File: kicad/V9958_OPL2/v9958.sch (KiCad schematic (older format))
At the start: 21 parts, among them U1 74LS139, U2 V9958, U3 DRAM_64KX4, U4 DRAM_64KX4, U5 DRAM_64KX4, U6 DRAM_64KX4, U7 DRAM_64KX4, U8 YM3812, U9 DRAM_64KX4, Y1 21,443Mhz

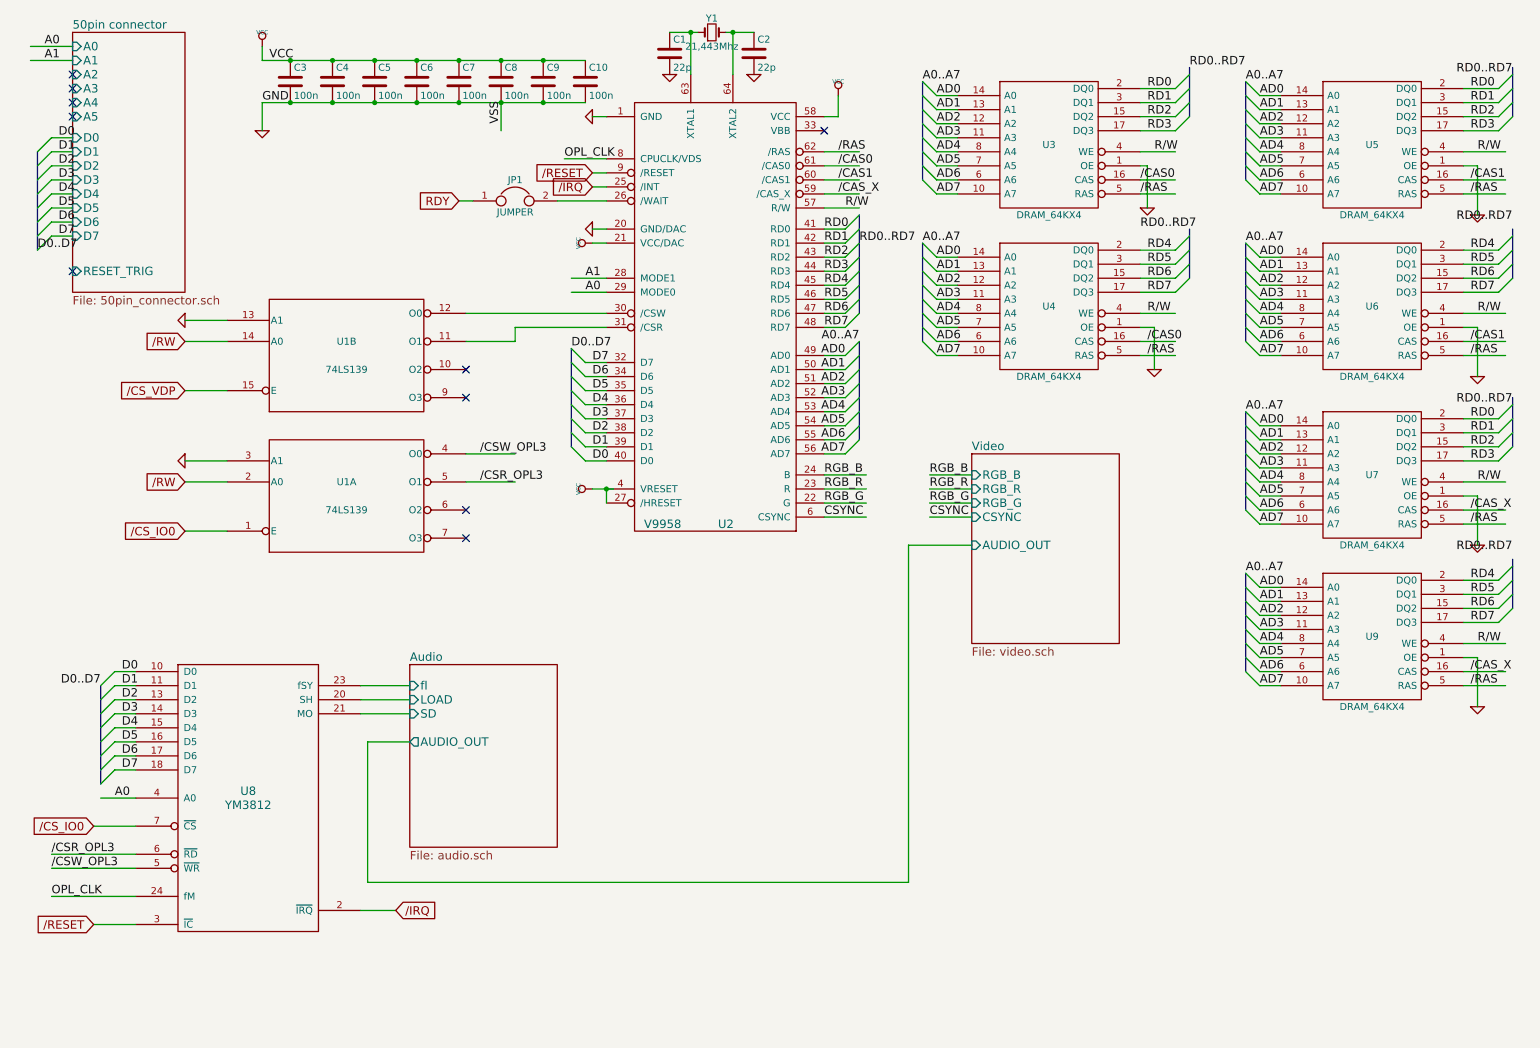
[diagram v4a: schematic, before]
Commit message: DRC fixes, filled areas
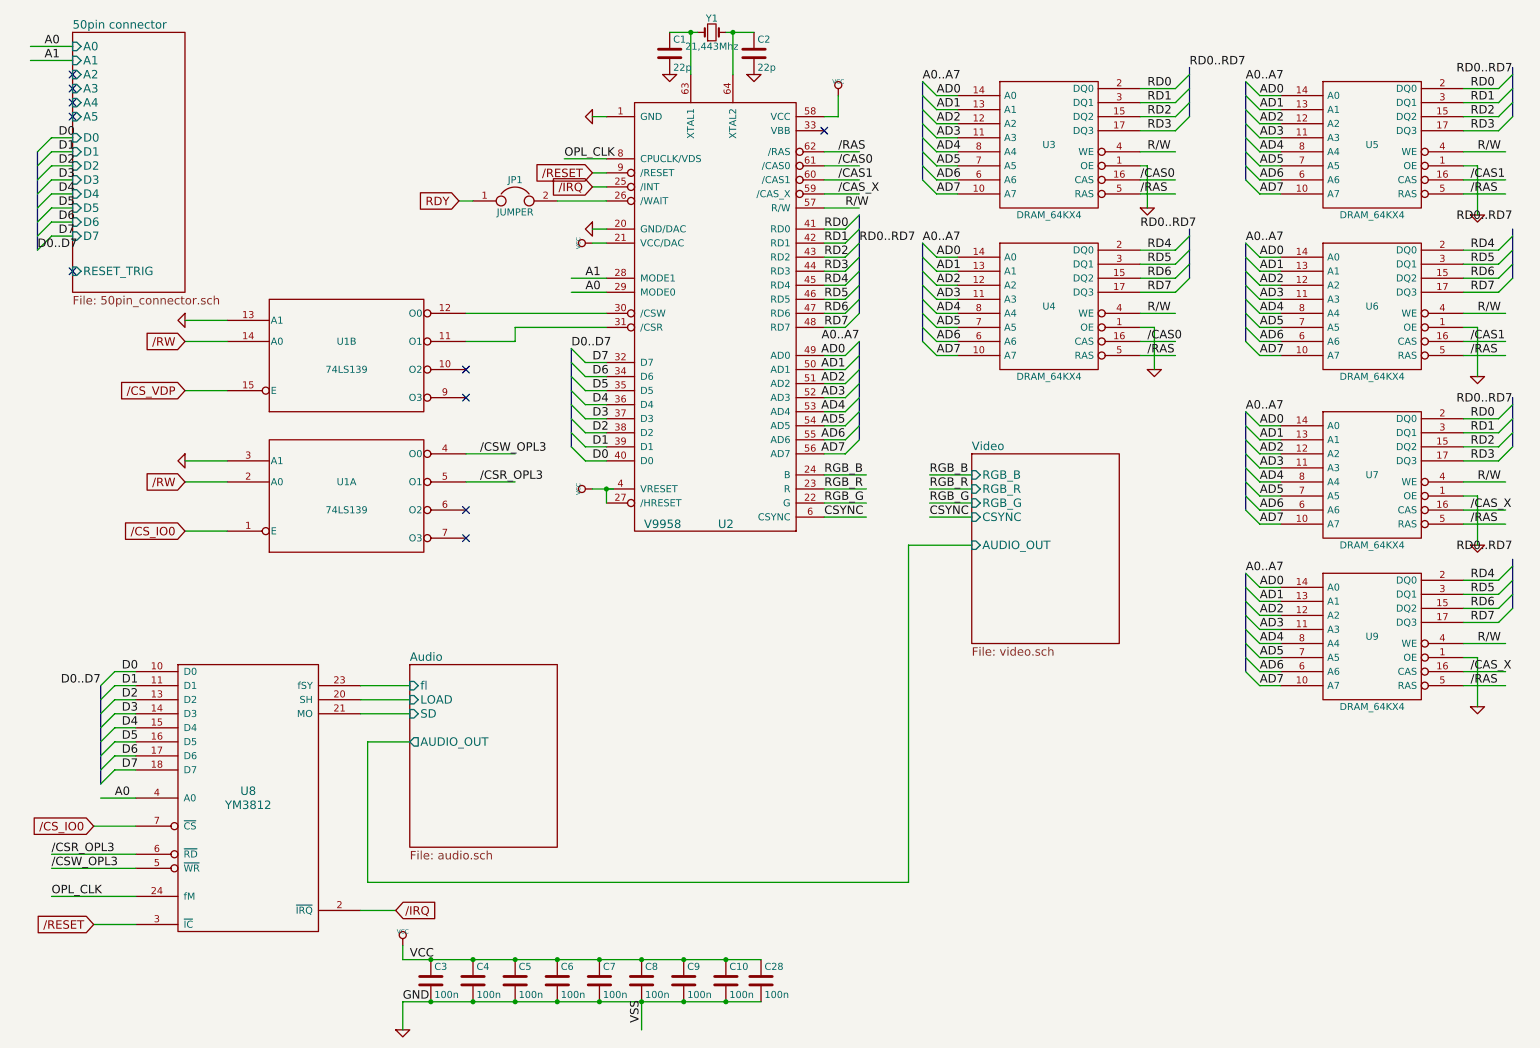
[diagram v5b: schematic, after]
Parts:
- added C28: 100n, Capacitors_ThroughHole:C_Disc_D3.0mm_W1.6mm_P2.50mm, symbol C
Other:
- moved on the sheet: C10, C3, C4, C5, C6, C7, C8, C9
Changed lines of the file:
@@
 Text Label 6350 1850 0    60   ~ 0
-R/W
-Text Label 8550 1450 0    60   ~ 0
-R/W
-Text Label 8500 2600 0    60   ~ 0
 R/W
 Text Label 10850 2600 0    60   ~ 0
@@
 L VCC #PWR010
 U 1 1 5A849B3A
-P 2200 700
-F 0 "#PWR010" H 2200 800 30  0001 C CNN
-F 1 "VCC" H 2200 800 30  0000 C CNN
-F 2 "" H 2200 700 60  0000 C CNN
-F 3 "" H 2200 700 60  0000 C CNN
-	1    2200 700
+P 3200 7100
+F 0 "#PWR010" H 3200 7200 30  0001 C CNN
+F 1 "VCC" H 3200 7200 30  0000 C CNN
+F 2 "" H 3200 7100 60  0000 C CNN
+F 3 "" H 3200 7100 60  0000 C CNN
+	1    3200 7100
 	1    0    0    -1
 $EndComp
@@
 L GND-RESCUE-v9958 #PWR011
 U 1 1 5A849BF6
-P 2200 1300
-F 0 "#PWR011" H 2200 1300 30  0001 C CNN
-F 1 "GND" H 2200 1230 30  0001 C CNN
-F 2 "" H 2200 1300 60  0000 C CNN
-F 3 "" H 2200 1300 60  0000 C CNN
-	1    2200 1300
+P 3200 7700
+F 0 "#PWR011" H 3200 7700 30  0001 C CNN
+F 1 "GND" H 3200 7630 30  0001 C CNN
+F 2 "" H 3200 7700 60  0000 C CNN
+F 3 "" H 3200 7700 60  0000 C CNN
+	1    3200 7700
 	1    0    0    -1
 $EndComp
@@
 L C C3
 U 1 1 5A84A455
-P 2400 950
-F 0 "C3" H 2425 1050 50  0000 L CNN
-F 1 "100n" H 2425 850 50  0000 L CNN
-F 2 "Capacitors_ThroughHole:C_Disc_D3.0mm_W1.6mm_P2.50mm" H 2438 800 50  0001 C CNN
-F 3 "" H 2400 950 50  0001 C CNN
-	1    2400 950
+P 3400 7350
+F 0 "C3" H 3425 7450 50  0000 L CNN
+F 1 "100n" H 3425 7250 50  0000 L CNN
+F 2 "Capacitors_ThroughHole:C_Disc_D3.0mm_W1.6mm_P2.50mm" H 3438 7200 50  0001 C CNN
+F 3 "" H 3400 7350 50  0001 C CNN
+	1    3400 7350
 	1    0    0    -1
 $EndComp
@@
 L C C4
 U 1 1 5A84B161
-P 2700 950
-F 0 "C4" H 2725 1050 50  0000 L CNN
-F 1 "100n" H 2725 850 50  0000 L CNN
-F 2 "Capacitors_ThroughHole:C_Disc_D3.0mm_W1.6mm_P2.50mm" H 2738 800 50  0001 C CNN
-F 3 "" H 2700 950 50  0001 C CNN
-	1    2700 950
+P 3700 7350
+F 0 "C4" H 3725 7450 50  0000 L CNN
+F 1 "100n" H 3725 7250 50  0000 L CNN
+F 2 "Capacitors_ThroughHole:C_Disc_D3.0mm_W1.6mm_P2.50mm" H 3738 7200 50  0001 C CNN
+F 3 "" H 3700 7350 50  0001 C CNN
+	1    3700 7350
 	1    0    0    -1
 $EndComp
@@
 L C C5
 U 1 1 5A84B232
-P 3000 950
-F 0 "C5" H 3025 1050 50  0000 L CNN
-F 1 "100n" H 3025 850 50  0000 L CNN
-F 2 "Capacitors_ThroughHole:C_Disc_D3.0mm_W1.6mm_P2.50mm" H 3038 800 50  0001 C CNN
-F 3 "" H 3000 950 50  0001 C CNN
-	1    3000 950
+P 4000 7350
+F 0 "C5" H 4025 7450 50  0000 L CNN
+F 1 "100n" H 4025 7250 50  0000 L CNN
+F 2 "Capacitors_ThroughHole:C_Disc_D3.0mm_W1.6mm_P2.50mm" H 4038 7200 50  0001 C CNN
+F 3 "" H 4000 7350 50  0001 C CNN
+	1    4000 7350
 	1    0    0    -1
 $EndComp
@@
 L C C6
 U 1 1 5A84B308
-P 3300 950
-F 0 "C6" H 3325 1050 50  0000 L CNN
-F 1 "100n" H 3325 850 50  0000 L CNN
-F 2 "Capacitors_ThroughHole:C_Disc_D3.0mm_W1.6mm_P2.50mm" H 3338 800 50  0001 C CNN
-F 3 "" H 3300 950 50  0001 C CNN
-	1    3300 950
+P 4300 7350
+F 0 "C6" H 4325 7450 50  0000 L CNN
+F 1 "100n" H 4325 7250 50  0000 L CNN
+F 2 "Capacitors_ThroughHole:C_Disc_D3.0mm_W1.6mm_P2.50mm" H 4338 7200 50  0001 C CNN
+F 3 "" H 4300 7350 50  0001 C CNN
+	1    4300 7350
 	1    0    0    -1
 $EndComp
@@
 L C C7
 U 1 1 5A84B3DF
-P 3600 950
-F 0 "C7" H 3625 1050 50  0000 L CNN
-F 1 "100n" H 3625 850 50  0000 L CNN
-F 2 "Capacitors_ThroughHole:C_Disc_D3.0mm_W1.6mm_P2.50mm" H 3638 800 50  0001 C CNN
-F 3 "" H 3600 950 50  0001 C CNN
-	1    3600 950
+P 4600 7350
+F 0 "C7" H 4625 7450 50  0000 L CNN
+F 1 "100n" H 4625 7250 50  0000 L CNN
+F 2 "Capacitors_ThroughHole:C_Disc_D3.0mm_W1.6mm_P2.50mm" H 4638 7200 50  0001 C CNN
+F 3 "" H 4600 7350 50  0001 C CNN
+	1    4600 7350
 	1    0    0    -1
 $EndComp
@@
 L C C8
 U 1 1 5A84B731
-P 3900 950
-F 0 "C8" H 3925 1050 50  0000 L CNN
-F 1 "100n" H 3925 850 50  0000 L CNN
-F 2 "Capacitors_ThroughHole:C_Disc_D3.0mm_W1.6mm_P2.50mm" H 3938 800 50  0001 C CNN
-F 3 "" H 3900 950 50  0001 C CNN
-	1    3900 950
-	1    0    0    -1
-$EndComp
-Text Label 2250 800  0    60   ~ 0
+P 4900 7350
+F 0 "C8" H 4925 7450 50  0000 L CNN
+F 1 "100n" H 4925 7250 50  0000 L CNN
+F 2 "Capacitors_ThroughHole:C_Disc_D3.0mm_W1.6mm_P2.50mm" H 4938 7200 50  0001 C CNN
+F 3 "" H 4900 7350 50  0001 C CNN
+	1    4900 7350
+	1    0    0    -1
+$EndComp
+Text Label 3250 7200 0    60   ~ 0
 VCC
-Text Label 2200 1100 0    60   ~ 0
+Text Label 3200 7500 0    60   ~ 0
 GND
 NoConn ~ 6200 1300
@@
 Text Label 9300 2900 0    60   ~ 0
 AD7
-Text Label 3900 1250 1    60   ~ 0
+Text Label 4900 7650 1    60   ~ 0
 VSS
 $Comp
@@
 	10750 1450 11050 1450
 Wire Wire Line
-	8700 2600 8450 2600
-Wire Wire Line
-	8450 1450 8700 1450
-Wire Wire Line
 	8450 1550 8500 1550
 Wire Wire Line
@@
 	6300 1200 6200 1200
 Wire Wire Line
-	2200 1300 2200 1100
-Wire Wire Line
-	2200 1100 4500 1100
-Connection ~ 2400 1100
-Wire Wire Line
-	2200 700  2200 800
-Wire Wire Line
-	2200 800  4500 800
-Connection ~ 2400 800
-Connection ~ 2700 800
-Connection ~ 3000 800
-Connection ~ 3300 800
-Connection ~ 3600 800
-Connection ~ 2700 1100
-Connection ~ 3000 1100
-Connection ~ 3300 1100
-Connection ~ 3600 1100
+	3200 7700 3200 7500
+Wire Wire Line
+	3200 7500 5750 7500
+Connection ~ 3400 7500
+Wire Wire Line
+	3200 7100 3200 7200
+Wire Wire Line
+	3200 7200 5750 7200
+Connection ~ 3400 7200
+Connection ~ 3700 7200
+Connection ~ 4000 7200
+Connection ~ 4300 7200
+Connection ~ 4600 7200
+Connection ~ 3700 7500
+Connection ~ 4000 7500
+Connection ~ 4300 7500
+Connection ~ 4600 7500
 Wire Wire Line
 	4550 2000 4650 2000
@@
 	9450 2900 9300 2900
 Wire Wire Line
-	3900 1100 3900 1300
+	4900 7500 4900 7700
 Wire Wire Line
 	1650 3150 1950 3150
@@
 L C C9
 U 1 1 5BE31936
-P 4200 950
-F 0 "C9" H 4225 1050 50  0000 L CNN
-F 1 "100n" H 4225 850 50  0000 L CNN
-F 2 "Capacitors_ThroughHole:C_Disc_D3.0mm_W1.6mm_P2.50mm" H 4238 800 50  0001 C CNN
-F 3 "" H 4200 950 50  0001 C CNN
-	1    4200 950
+P 5200 7350
+F 0 "C9" H 5225 7450 50  0000 L CNN
+F 1 "100n" H 5225 7250 50  0000 L CNN
+F 2 "Capacitors_ThroughHole:C_Disc_D3.0mm_W1.6mm_P2.50mm" H 5238 7200 50  0001 C CNN
+F 3 "" H 5200 7350 50  0001 C CNN
+	1    5200 7350
 	1    0    0    -1
 $EndComp
@@
 L C C10
 U 1 1 5BE31A15
-P 4500 950
-F 0 "C10" H 4525 1050 50  0000 L CNN
-F 1 "100n" H 4525 850 50  0000 L CNN
-F 2 "Capacitors_ThroughHole:C_Disc_D3.0mm_W1.6mm_P2.50mm" H 4538 800 50  0001 C CNN
-F 3 "" H 4500 950 50  0001 C CNN
-	1    4500 950
-	1    0    0    -1
-$EndComp
-Connection ~ 3900 800
-Connection ~ 4200 800
-Connection ~ 3900 1100
-Connection ~ 4200 1100
+P 5500 7350
+F 0 "C10" H 5525 7450 50  0000 L CNN
+F 1 "100n" H 5525 7250 50  0000 L CNN
+F 2 "Capacitors_ThroughHole:C_Disc_D3.0mm_W1.6mm_P2.50mm" H 5538 7200 50  0001 C CNN
+F 3 "" H 5500 7350 50  0001 C CNN
+	1    5500 7350
+	1    0    0    -1
+$EndComp
+Connection ~ 4900 7200
+Connection ~ 5200 7200
+Connection ~ 4900 7500
+Connection ~ 5200 7500
 Wire Wire Line
 	3250 5650 2950 5650
@@
 Wire Wire Line
 	6800 4250 7250 4250
+Wire Wire Line
+	8450 1450 8700 1450
+Text Label 8500 1450 0    60   ~ 0
+R/W
+Wire Wire Line
+	8450 2600 8700 2600
+Text Label 8500 2600 0    60   ~ 0
+R/W
+$Comp
+L C C28
+U 1 1 5BF21DF3
+P 5750 7350
+F 0 "C28" H 5775 7450 50  0000 L CNN
+F 1 "100n" H 5775 7250 50  0000 L CNN
+F 2 "Capacitors_ThroughHole:C_Disc_D3.0mm_W1.6mm_P2.50mm" H 5788 7200 50  0001 C CNN
+F 3 "" H 5750 7350 50  0001 C CNN
+	1    5750 7350
+	1    0    0    -1
+$EndComp
+Connection ~ 5500 7200
+Connection ~ 5500 7500
 $EndSCHEMATC

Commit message: footprint
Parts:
- JP1: footprint Pin_Headers:Pin_Header_Straight_1x02 -> Pin_Headers:Pin_Header_Straight_1x02_Pitch2.54mm
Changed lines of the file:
@@
 F 0 "JP1" H 4000 1950 50  0000 C CNN
 F 1 "JUMPER" H 4000 1720 50  0000 C CNN
-F 2 "Pin_Headers:Pin_Header_Straight_1x02" H 4000 1800 50  0001 C CNN
+F 2 "Pin_Headers:Pin_Header_Straight_1x02_Pitch2.54mm" H 4000 1800 50  0001 C CNN
 F 3 "" H 4000 1800 50  0000 C CNN
 	1    4000 1800
@@
 Wire Wire Line
 	7150 1750 7000 1750
-Wire Bus Line
-	6900 2100 6900 2800
 Wire Wire Line
 	7000 2200 7150 2200

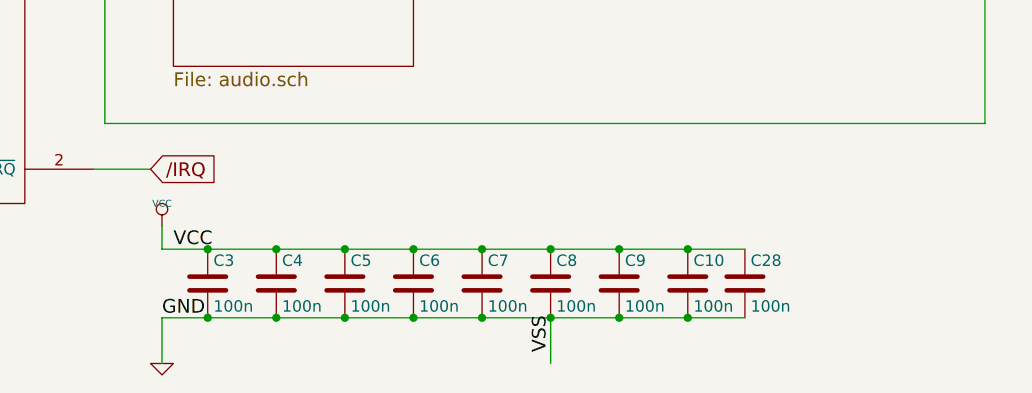
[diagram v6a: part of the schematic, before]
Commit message: bypass capacitor for opamp, routing fixes/opt.
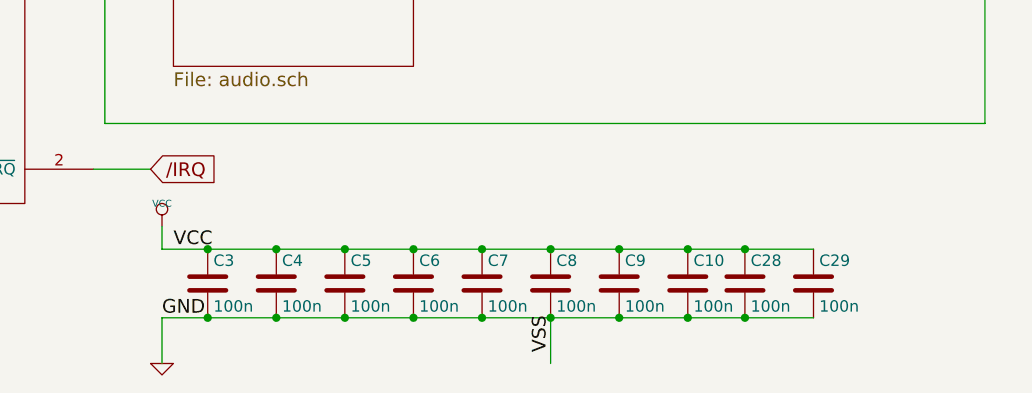
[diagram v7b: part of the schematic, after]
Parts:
- added C29: 100n, Capacitors_ThroughHole:C_Disc_D3.0mm_W1.6mm_P2.50mm, symbol C
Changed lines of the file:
@@
 	3200 7700 3200 7500
 Wire Wire Line
-	3200 7500 5750 7500
+	3200 7500 6050 7500
 Connection ~ 3400 7500
 Wire Wire Line
 	3200 7100 3200 7200
 Wire Wire Line
-	3200 7200 5750 7200
+	3200 7200 6050 7200
 Connection ~ 3400 7200
 Connection ~ 3700 7200
@@
 Connection ~ 5500 7200
 Connection ~ 5500 7500
+$Comp
+L C C29
+U 1 1 5BF84816
+P 6050 7350
+F 0 "C29" H 6075 7450 50  0000 L CNN
+F 1 "100n" H 6075 7250 50  0000 L CNN
+F 2 "Capacitors_ThroughHole:C_Disc_D3.0mm_W1.6mm_P2.50mm" H 6088 7200 50  0001 C CNN
+F 3 "" H 6050 7350 50  0001 C CNN
+	1    6050 7350
+	1    0    0    -1
+$EndComp
+Connection ~ 5750 7200
+Connection ~ 5750 7500
 $EndSCHEMATC

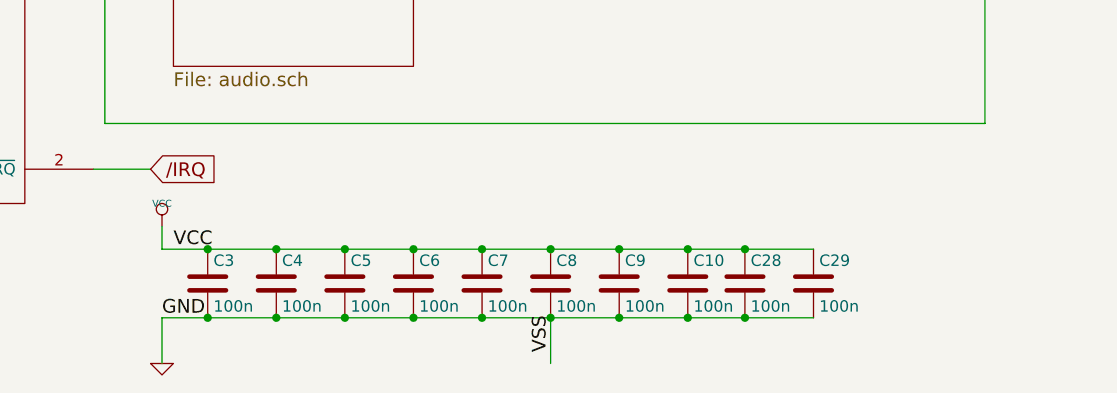
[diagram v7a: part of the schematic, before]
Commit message: extra cap, small fixes, silkscreen, enablen B.Silk
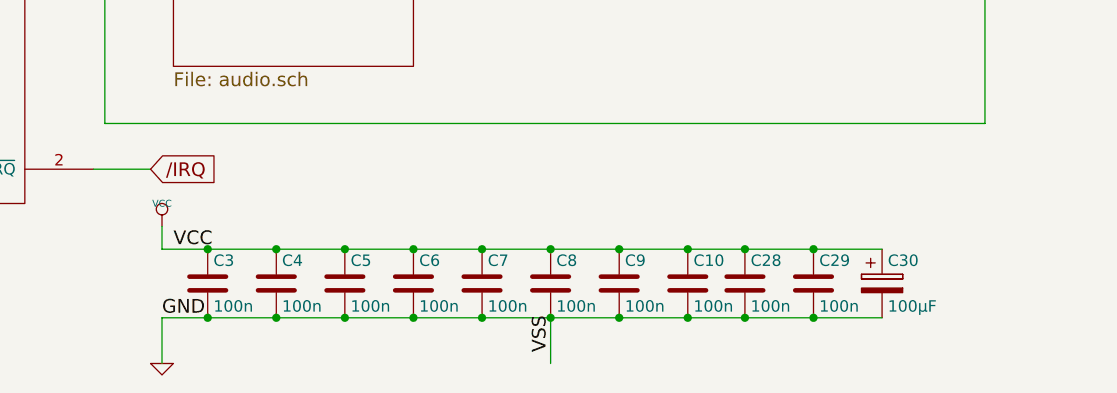
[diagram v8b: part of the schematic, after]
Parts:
- added C30: 100µF, symbol CP
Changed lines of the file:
@@
 	3200 7700 3200 7500
 Wire Wire Line
-	3200 7500 6050 7500
+	3200 7500 6350 7500
 Connection ~ 3400 7500
 Wire Wire Line
 	3200 7100 3200 7200
 Wire Wire Line
-	3200 7200 6050 7200
+	3200 7200 6350 7200
 Connection ~ 3400 7200
 Connection ~ 3700 7200
@@
 Connection ~ 5750 7200
 Connection ~ 5750 7500
+$Comp
+L CP C30
+U 1 1 5C085F77
+P 6350 7350
+F 0 "C30" H 6375 7450 50  0000 L CNN
+F 1 "100µF" H 6375 7250 50  0000 L CNN
+F 2 "" H 6388 7200 50  0001 C CNN
+F 3 "" H 6350 7350 50  0001 C CNN
+	1    6350 7350
+	1    0    0    -1
+$EndComp
+Connection ~ 6050 7200
+Connection ~ 6050 7500
 $EndSCHEMATC
